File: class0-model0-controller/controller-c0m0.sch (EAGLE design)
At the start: 11 parts, among them U1 TPS2378

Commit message: Add auxiliary power supplies
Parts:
- added C2, C7: 100nF, rcl:C-EUC0805
- added C3, C8, C9: 10uF, rcl:CPOL-EUA/3216-18R
- added D3, D4: BAT60J, diode:BAT60J
- added D5, D6: 1N4148, diode:DIODE-SOD323-W
- added IC1, IC3: MCP16301/H, MCP16301:MCP16301/H
- added L1, L2: 15uH, rcl:L-USPIS2816
- added R11: 50K, rcl:R-EU_R0805
- added R12: 10K, rcl:R-EU_R0805
- added R5: 50K, resistor:R-TRIMM3314G
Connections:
- new net +5VDC: C8.+, C9.+, D5.A, L1.2, R11.2
- new net +V_LOCK: C3.+, D6.A, L2.2
- new net N$22: C7.2, D4.C, IC3.SW, L1.1
- new net N$23: C7.1, D5.C, IC3.BOOST
- new net N$25: IC3.VFB, R11.1, R12.2
- new net N$4: C2.2, D3.C, IC1.SW, L2.1
- new net N$6: C2.1, D6.C, IC1.BOOST
- new net N$7: IC1.VFB
- net +24VDC: now also IC1.EN, IC1.VIN, IC3.EN, IC3.VIN
- net GND: now also C3.-, C8.-, C9.-, D3.A, D4.A, IC1.GND, IC3.GND, R12.1, R5.E
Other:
- note added: "24VDC Power Over Ethernet Power Supply Segment"
- note added: "5VDC Logic Power Supply"
- note added: "Lock power supply"
- note removed: "24VDC POE Power Supply Segment"

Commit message: Add relays section
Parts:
- added JP-LOCK, JP_HOLD_OPEN: (no value), SparkFun:M05PTH_LONGPADS
- added K1, K2: HE751, relay:HE751
- added Q1, Q2: BS170, transistor-small-signal:BS170
- added R6, R7: 10K, eagle-ltspice:R
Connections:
- new net HOLD: Q2.G, R6.1
- new net LOCK: Q1.G, R7.1
- new net N$10: JP_HOLD_OPEN.3, K22.S
- new net N$11: JP_HOLD_OPEN.4, K22.P
- new net N$12: K11.2, Q1.D
- new net N$13: K21.2, Q2.D
- new net N$8: JP-LOCK.3, K12.S
- new net N$9: JP-LOCK.4, K12.P
- net +24VDC: now also JP-LOCK.1, JP_HOLD_OPEN.1
- net +5VDC: now also K11.1, K21.1
- net +V_LOCK: now also JP-LOCK.2, JP_HOLD_OPEN.2, R5.A
- net GND: now also JP-LOCK.5, JP_HOLD_OPEN.5, Q1.S, Q2.S, R6.2, R7.2
- net N$7: now also R5.S
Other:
- note added: "Lock and Hold-Open relays"

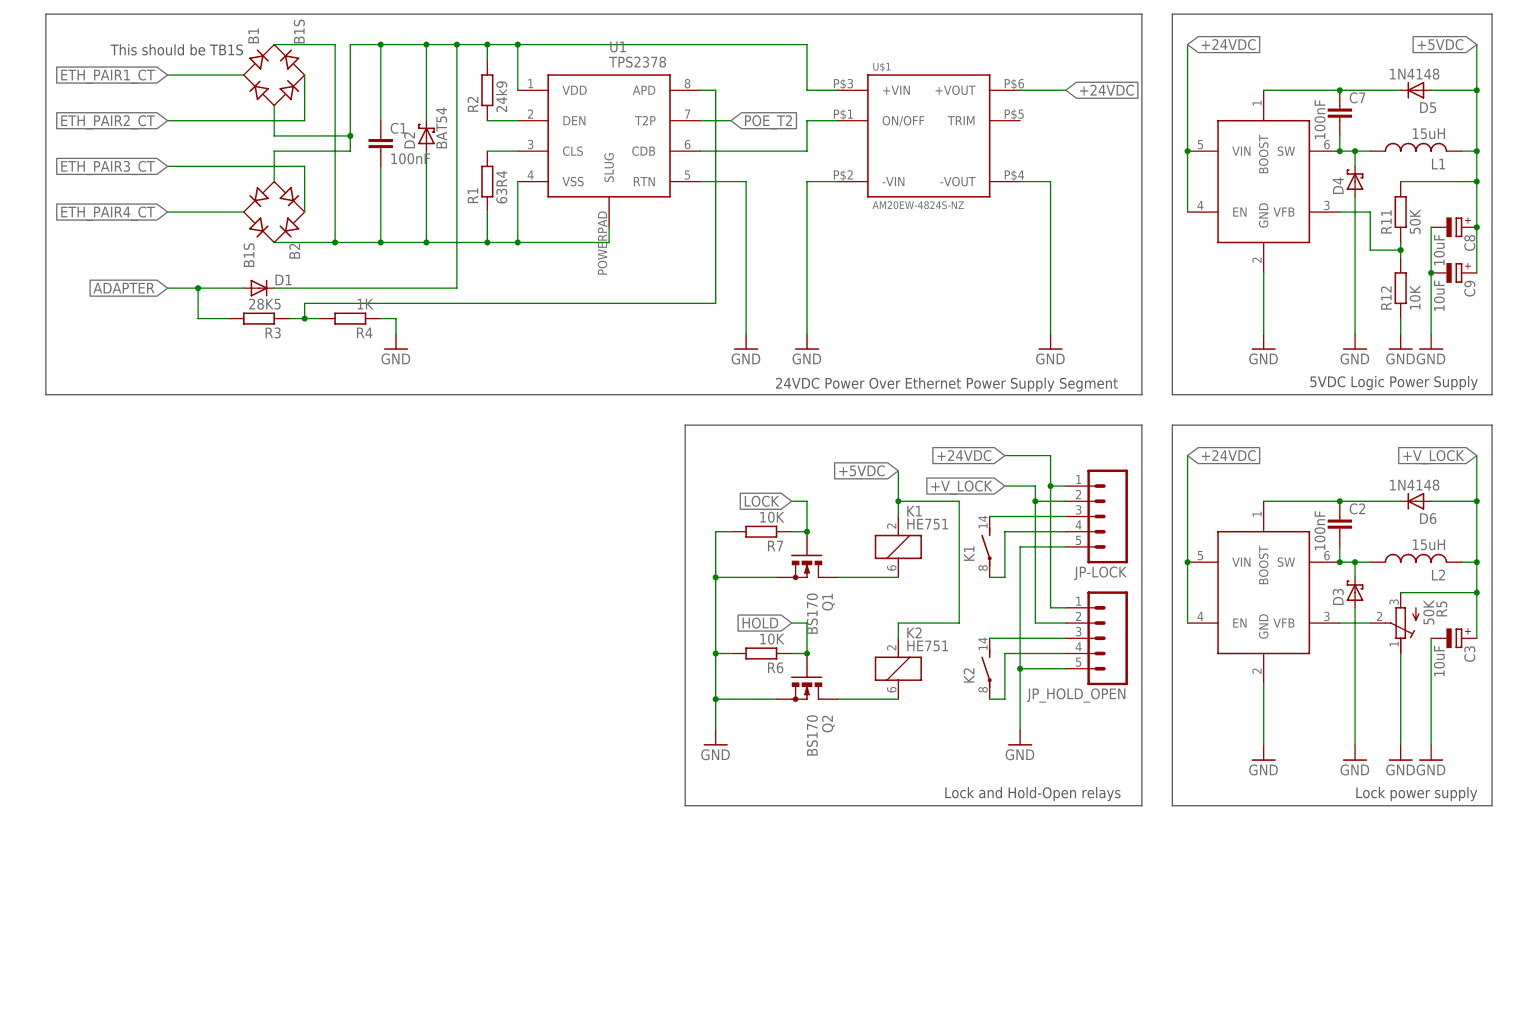
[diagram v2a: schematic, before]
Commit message: Add Door Open contact input protection
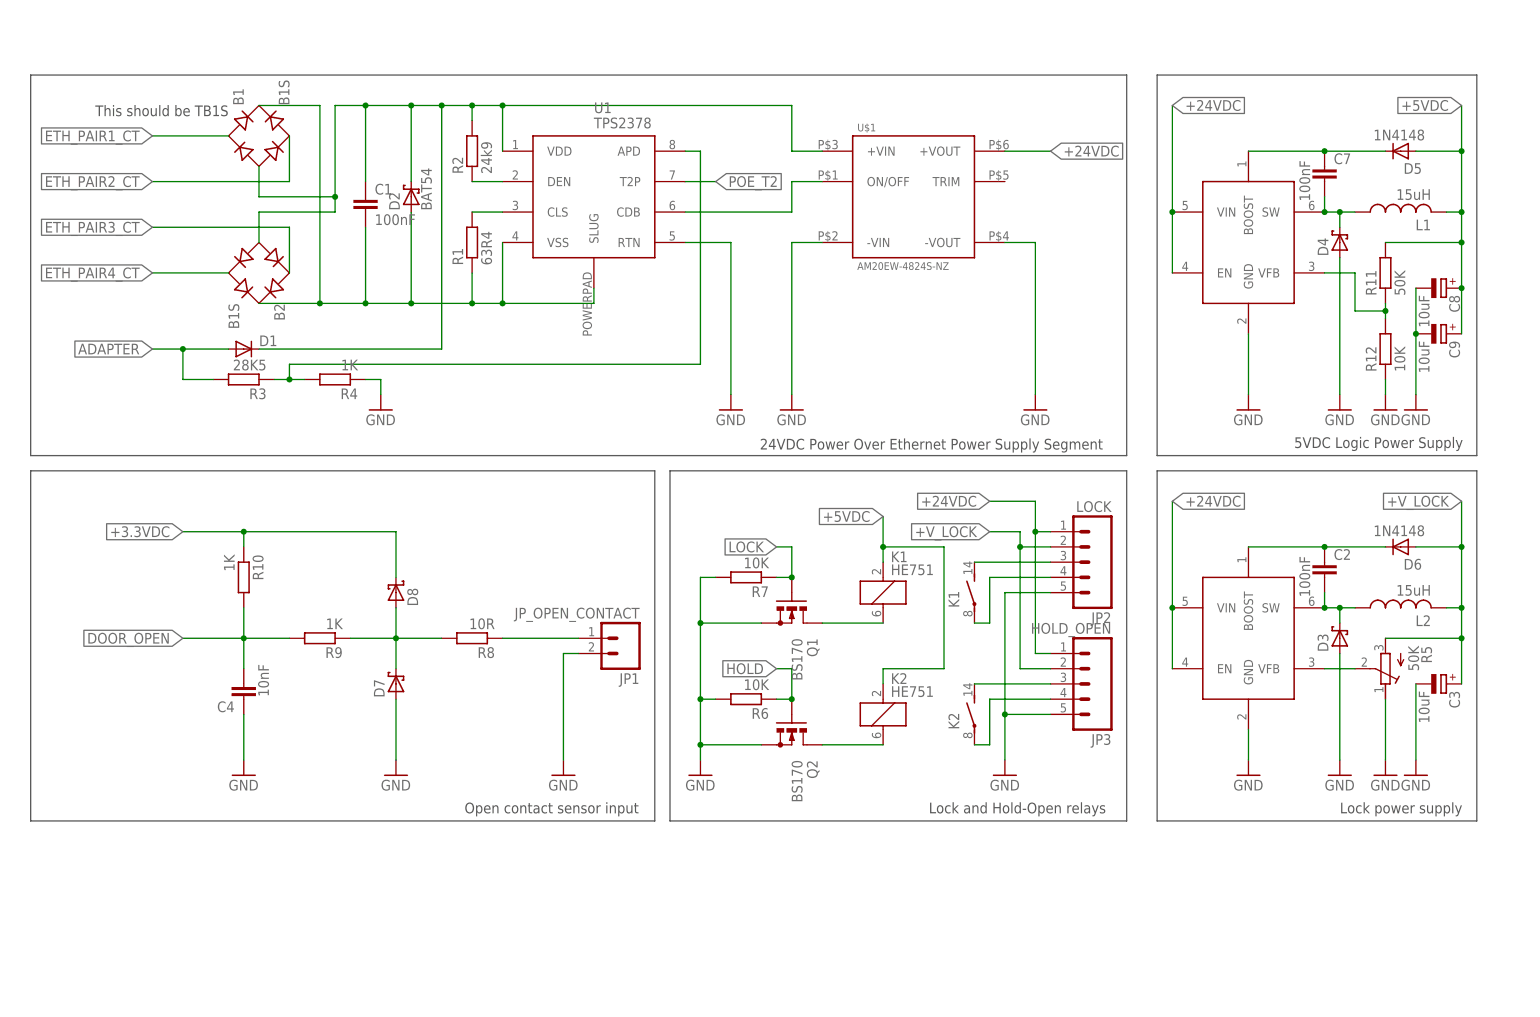
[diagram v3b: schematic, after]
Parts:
- removed JP-LOCK, JP_HOLD_OPEN: (no value), SparkFun:M05PTH_LONGPADS
- added C4: 10nF, rcl:C-EUC0805
- added D7, D8: BAT60J, diode:BAT60J
- added JP1: JP_OPEN_CONTACT, SparkFun:M02LOCK_LONGPADS
- added JP2: LOCK, SparkFun:M05PTH_LONGPADS
- added JP3: HOLD_OPEN, SparkFun:M05PTH_LONGPADS
- added R10, R9: 1K, rcl:R-EU_R0805
- added R8: 10R, rcl:R-EU_R0805
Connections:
- new net +3.3VDC: D8.C, R10.1
- new net DOOR_OPEN: C4.2, R10.2, R9.2
- new net N$14: D7.C, D8.A, R8.2, R9.1
- new net N$16: JP1.1, R8.1
- net +24VDC: now also JP2.1, JP3.1; no longer JP-LOCK.1, JP_HOLD_OPEN.1
- net +V_LOCK: now also JP2.2, JP3.2; no longer JP-LOCK.2, JP_HOLD_OPEN.2
- net GND: now also C4.1, D7.A, JP1.2, JP2.5, JP3.5; no longer JP-LOCK.5, JP_HOLD_OPEN.5
- net N$10: now also JP3.3; no longer JP_HOLD_OPEN.3
- net N$11: now also JP3.4; no longer JP_HOLD_OPEN.4
- net N$8: now also JP2.3; no longer JP-LOCK.3
- net N$9: now also JP2.4; no longer JP-LOCK.4
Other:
- note added: "Open contact sensor input"
- moved on the sheet: B1, B2, C1, C2, C3, C7, C8, C9, D1, D2, D3, D4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

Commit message: Add interface to two Readers
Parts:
- added C10, C11, C13, C14: 1uF, rcl:C-EUC0805
- added IC4: MAX3232CSE, maxim:MAX3232CSE
- added J1, J2: RJ12 6p6c, con-tycoelectronics:RJ11-2X
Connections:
- new net N$15: IC4G$1.T1OUT, J1.3
- new net N$17: IC4G$1.R1IN, J1.4
- new net N$18: C10.1, IC4G$1.C1+
- new net N$19: C10.2, IC4G$1.C1-
- new net N$20: C11.1, IC4G$1.C2+
- new net N$21: C11.2, IC4G$1.C2-
- new net N$24: C13.1, IC4G$1.V+
- new net N$26: C14.1, IC4G$1.V-
- new net N$27: IC4G$1.T2OUT, J2.3
- new net N$29: IC4G$1.R2IN, J2.4
- new net RDR1_BOOT: J1.6
- new net RDR1_RST: J1.2
- new net RDR2_BOOT: J2.6
- new net RDR2_RST: J2.2
- net +24VDC: now also J1.1, J2.1
- net +3.3VDC: now also C13.2, IC4P.VCC
- net GND: now also C14.2, IC4P.GND, J1.5, J2.5
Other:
- note added: "Interface to Readers"
- note added: "Note: Eagle labels have the following format: LABEL_NAME/<SHEET>.<COORDINATES> So +5VDC/2.1A does NOT meat 2.1 Amps, but that it is connected to Sheet 2 in section 1A"

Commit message: Add Ethernet interface to schematic
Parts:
- added C5: 100nF, rcl:C-EUC0805
- added U$2: 0813-1X1T-57-F, con-belfuse:0813-1X1T-57-F
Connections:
- new net ETH_RXN: U$2.RD-
- new net ETH_RXP: U$2.RD+
- new net ETH_TXN: U$2.TD-
- new net ETH_TXP: U$2.TD+
- new net N$28: C5.2, U$2.CT
- net ETH_PAIR1_CT: now also U$2.VC2+
- net ETH_PAIR2_CT: now also B2.AC2, U$2.VC1+; no longer B1.AC2
- net ETH_PAIR3_CT: now also U$2.VC1-
- net ETH_PAIR4_CT: now also B1.AC2, U$2.VC2-; no longer B2.AC2
- net GND: now also C5.1, U$2.5
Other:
- note added: "Ethernet interface"
- moved on the sheet: C10, C11, C13, C14, IC4, IC4P, J1, J2

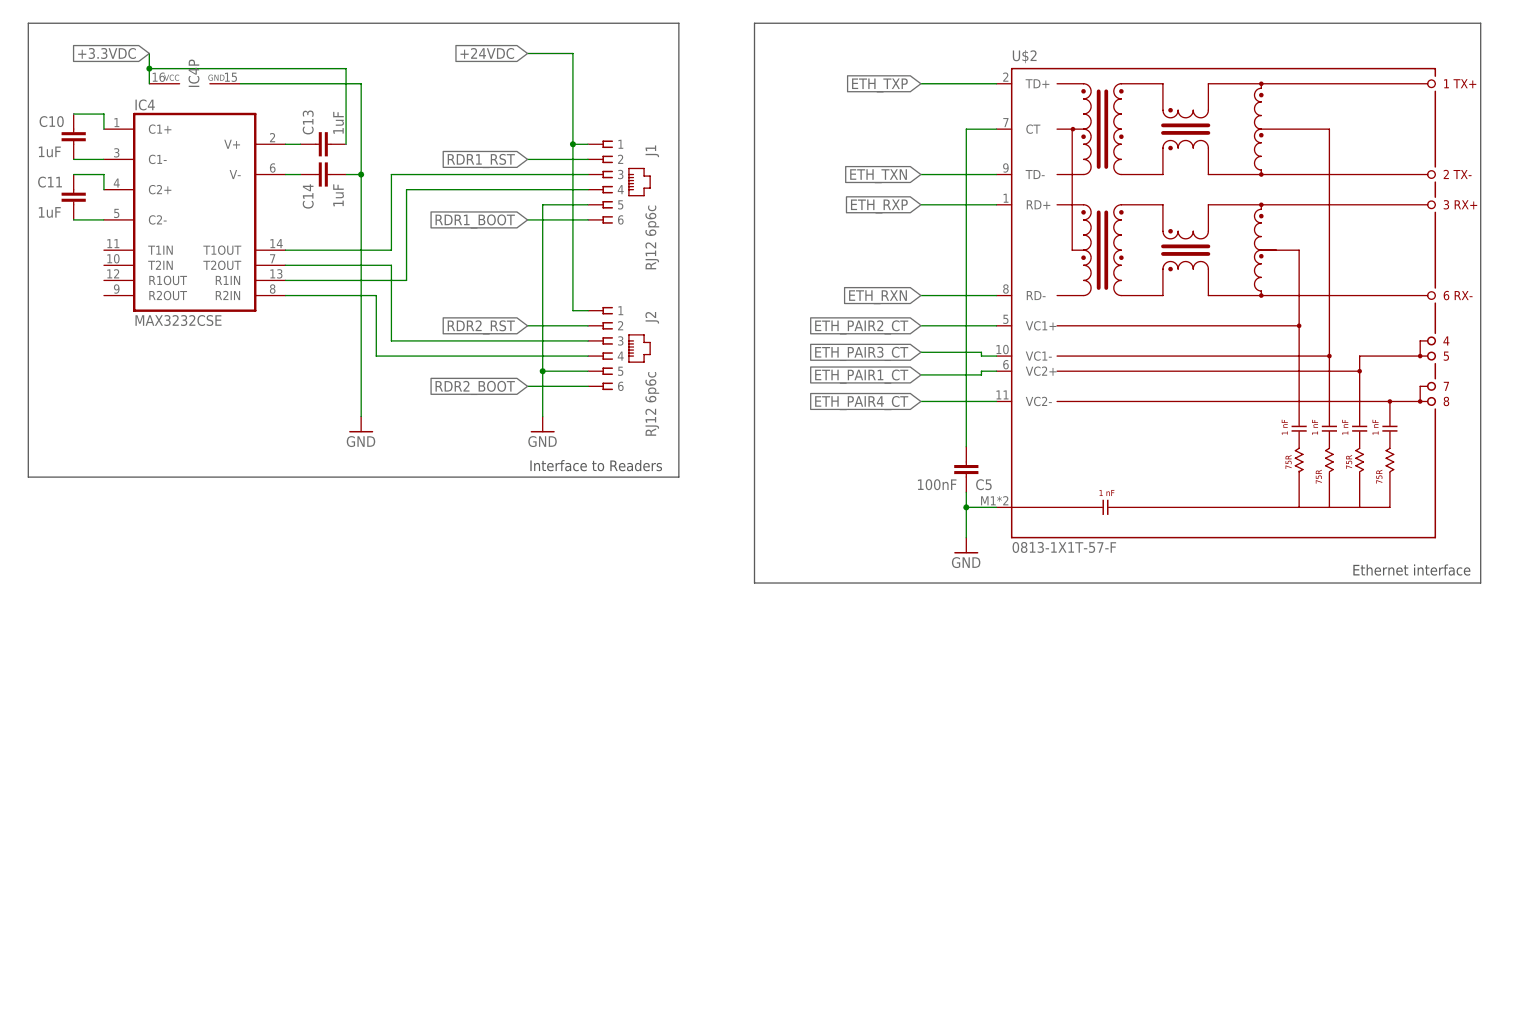
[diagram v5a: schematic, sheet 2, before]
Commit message: Add primary control circuitry
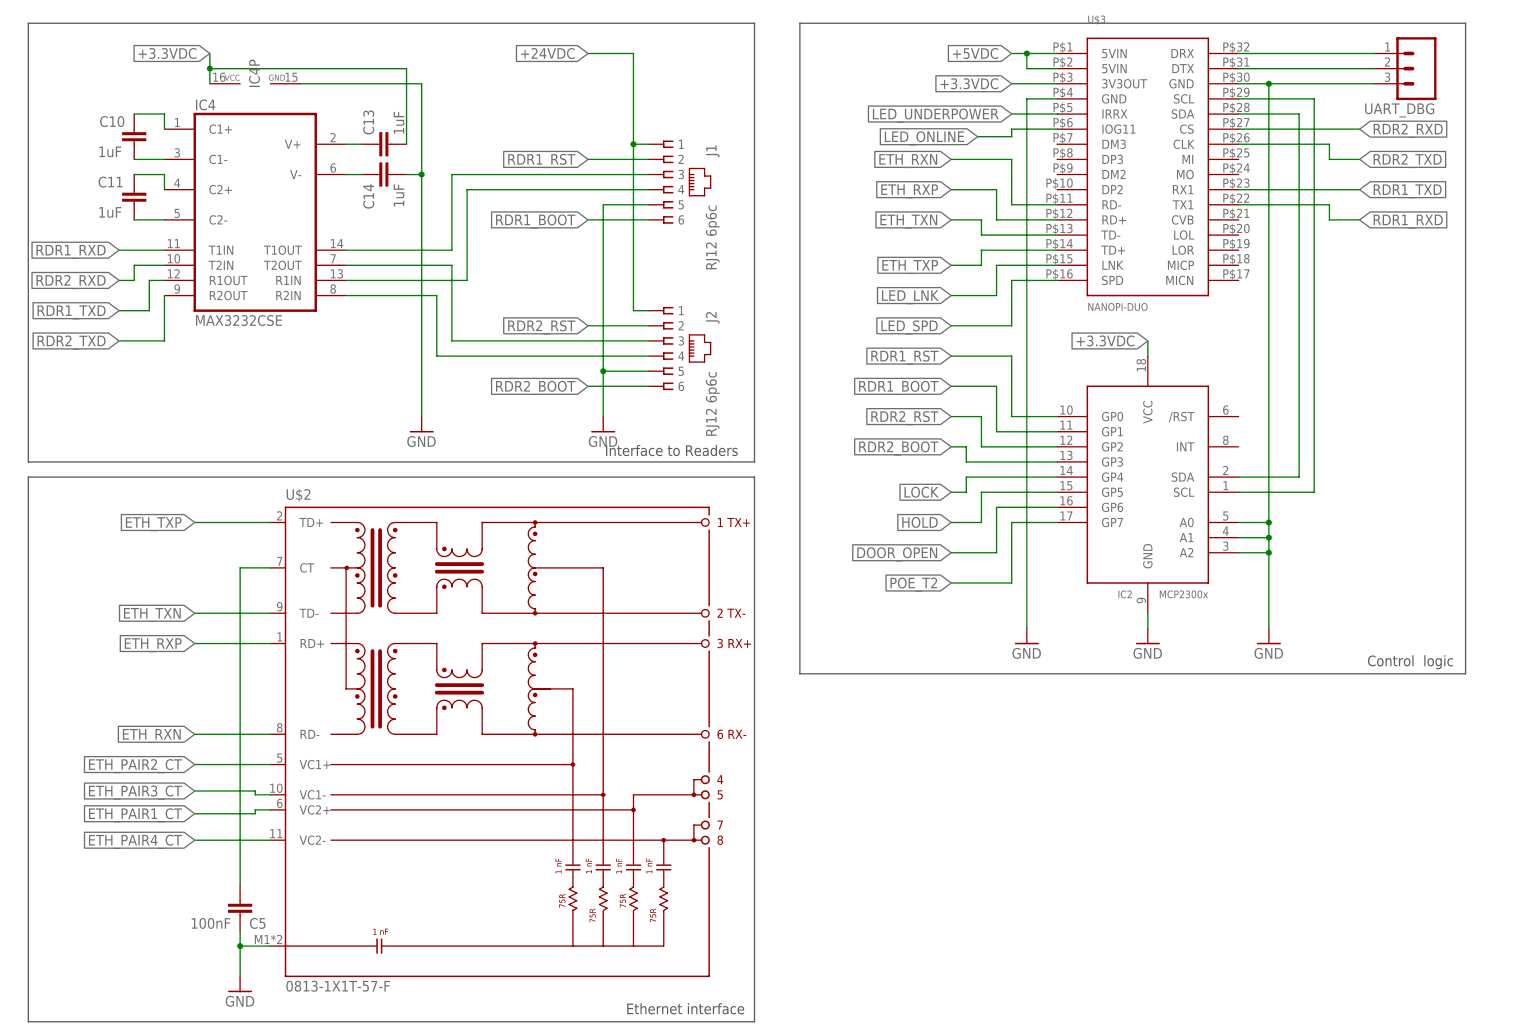
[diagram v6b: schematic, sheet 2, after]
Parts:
- added IC2: MCP23008/SO, adafruit:MCP23008/SO
- added U$3: NANOPI-DUO, FriendlyARM:NANOPI-DUO
- added UART_DBG: (no value), SparkFun:M03LONGPADS
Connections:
- new net LED_LNK: U$3.LNK
- new net LED_ONLINE: U$3.IOG11
- new net LED_SPD: U$3.SPD
- new net LED_UNDERPOWER: U$3.IRRX
- new net N$30: IC2.SDA, U$3.SDA
- new net N$31: IC2.SCL, U$3.SCL
- new net N$33: U$3.DTX, UART_DBG.2
- new net N$34: U$3.DRX, UART_DBG.1
- new net RDR1_RXD: IC4G$1.T1IN, U$3.TX1
- new net RDR1_TXD: IC4G$1.R1OUT, U$3.RX1
- new net RDR2_RXD: IC4G$1.T2IN, U$3.CS
- new net RDR2_TXD: IC4G$1.R2OUT, U$3.CLK
- net +3.3VDC: now also IC2.VCC, U$3.3V3OUT
- net +5VDC: now also U$3.5VIN@1, U$3.5VIN@2
- net DOOR_OPEN: now also IC2.GP6
- net ETH_RXN: now also U$3.RD-
- net ETH_RXP: now also U$3.RD+
- net ETH_TXN: now also U$3.TD-
- net ETH_TXP: now also U$3.TD+
- net GND: now also IC2.A0, IC2.A1, IC2.A2, IC2.GND, U$3.GND@1, U$3.GND@2, UART_DBG.3
- net HOLD: now also IC2.GP5
- net LOCK: now also IC2.GP4
- net POE_T2: now also IC2.GP7
- net RDR1_BOOT: now also IC2.GP1
- net RDR1_RST: now also IC2.GP0
- net RDR2_BOOT: now also IC2.GP3
- net RDR2_RST: now also IC2.GP2
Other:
- note added: "Control logic"
- moved on the sheet: C10, C11, C13, C14, C5, IC4, IC4P, J1, J2, U$2

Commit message: Add LEDs
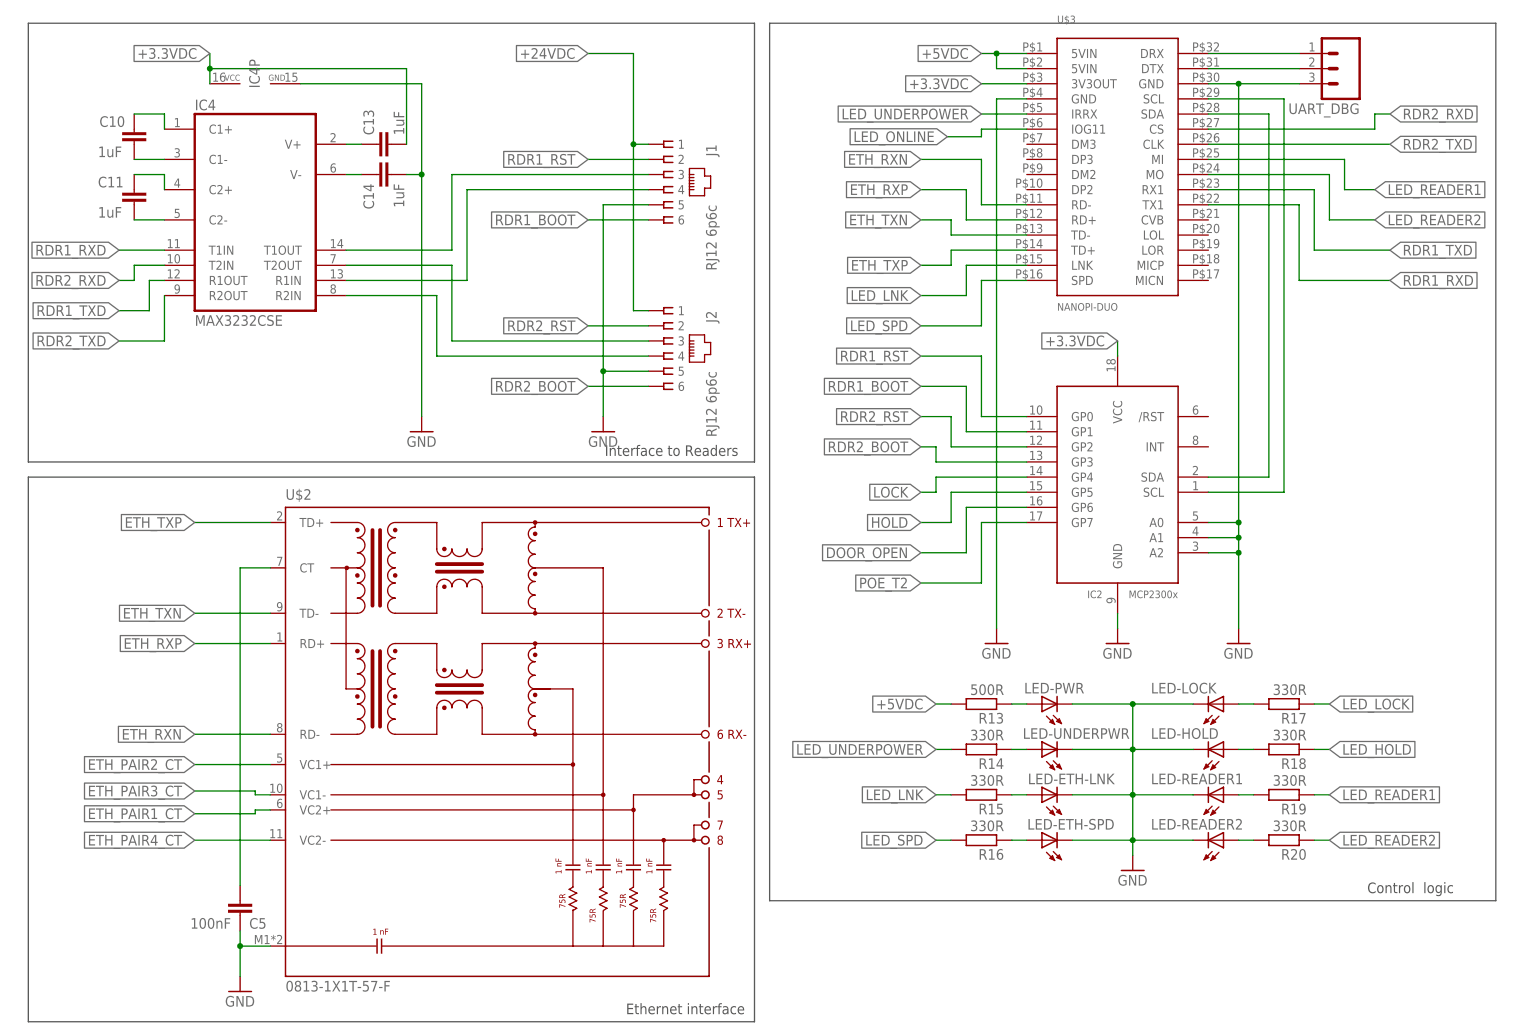
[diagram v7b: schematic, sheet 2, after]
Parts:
- added LED-ETH-LNK, LED-ETH-SPD, LED-HOLD, LED-LOCK, LED-PWR, LED-READER1, LED-READER2, LED-UNDERPWR: (no value), adafruit:LEDCHIP-LED0805
- added R13: 500R, eagle-ltspice:R
- added R14, R15, R16, R17, R18, R19, R20: 330R, eagle-ltspice:R
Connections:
- new net LED_HOLD: R18.1
- new net LED_LOCK: R17.1
- new net LED_READER1: R19.1, U$3.MI
- new net LED_READER2: R20.1, U$3.MO
- new net N$38: LED-PWR.A, R13.1
- new net N$39: LED-UNDERPWR.A, R14.1
- new net N$40: LED-ETH-LNK.A, R15.1
- new net N$41: LED-ETH-SPD.A, R16.1
- new net N$42: LED-LOCK.A, R17.2
- new net N$43: LED-HOLD.A, R18.2
- new net N$44: LED-READER1.A, R19.2
- new net N$45: LED-READER2.A, R20.2
- net +5VDC: now also R13.2
- net GND: now also LED-ETH-LNK.C, LED-ETH-SPD.C, LED-HOLD.C, LED-LOCK.C, LED-PWR.C, LED-READER1.C, LED-READER2.C, LED-UNDERPWR.C
- net LED_LNK: now also R15.2
- net LED_SPD: now also R16.2
- net LED_UNDERPOWER: now also R14.2
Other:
- moved on the sheet: IC2, U$3, UART_DBG
